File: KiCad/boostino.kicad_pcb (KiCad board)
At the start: 2 copper layers, 87.6 x 50.8 mm, 13 parts, among them J1 Conn_01x14_Female, J2 Conn_01x04_Male, Q1 2N3904, U1 Teensy3.6

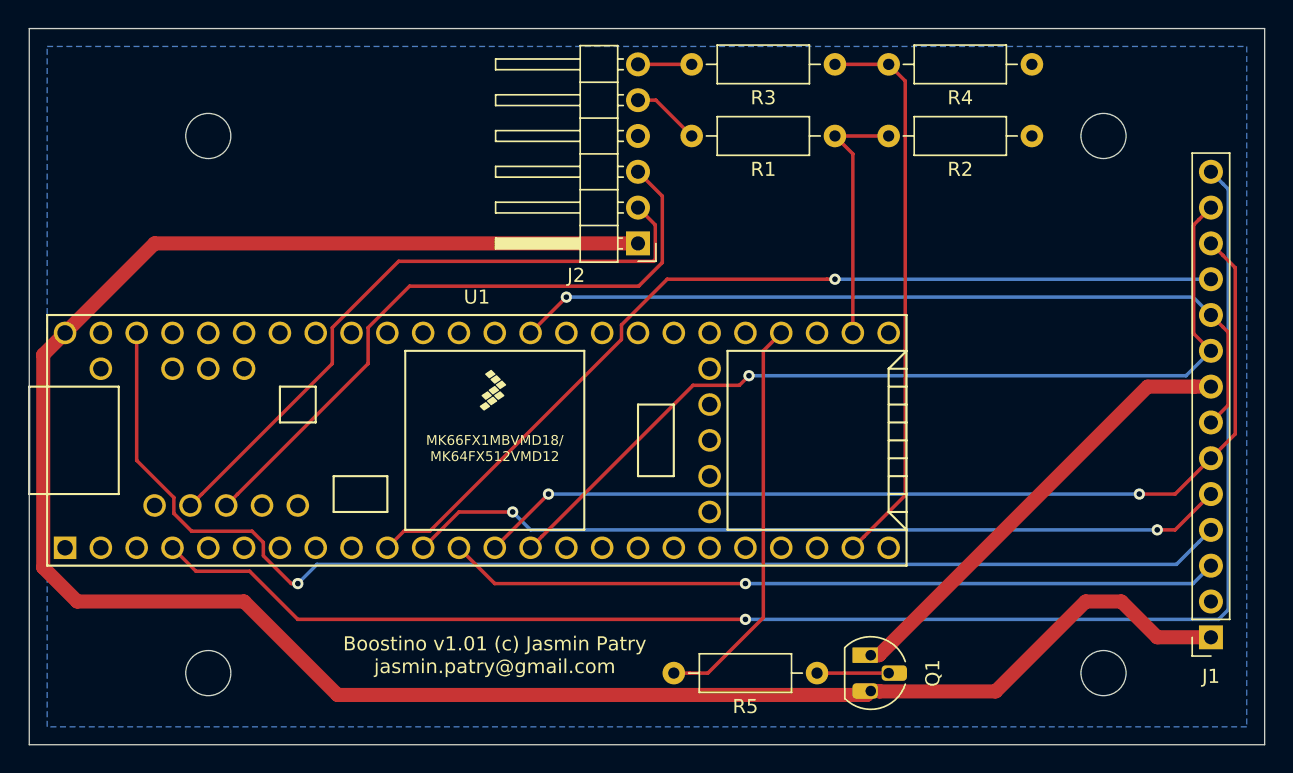
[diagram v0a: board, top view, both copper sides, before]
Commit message: Updated PCB for MC33660. Still need to regenerate Gerber files.
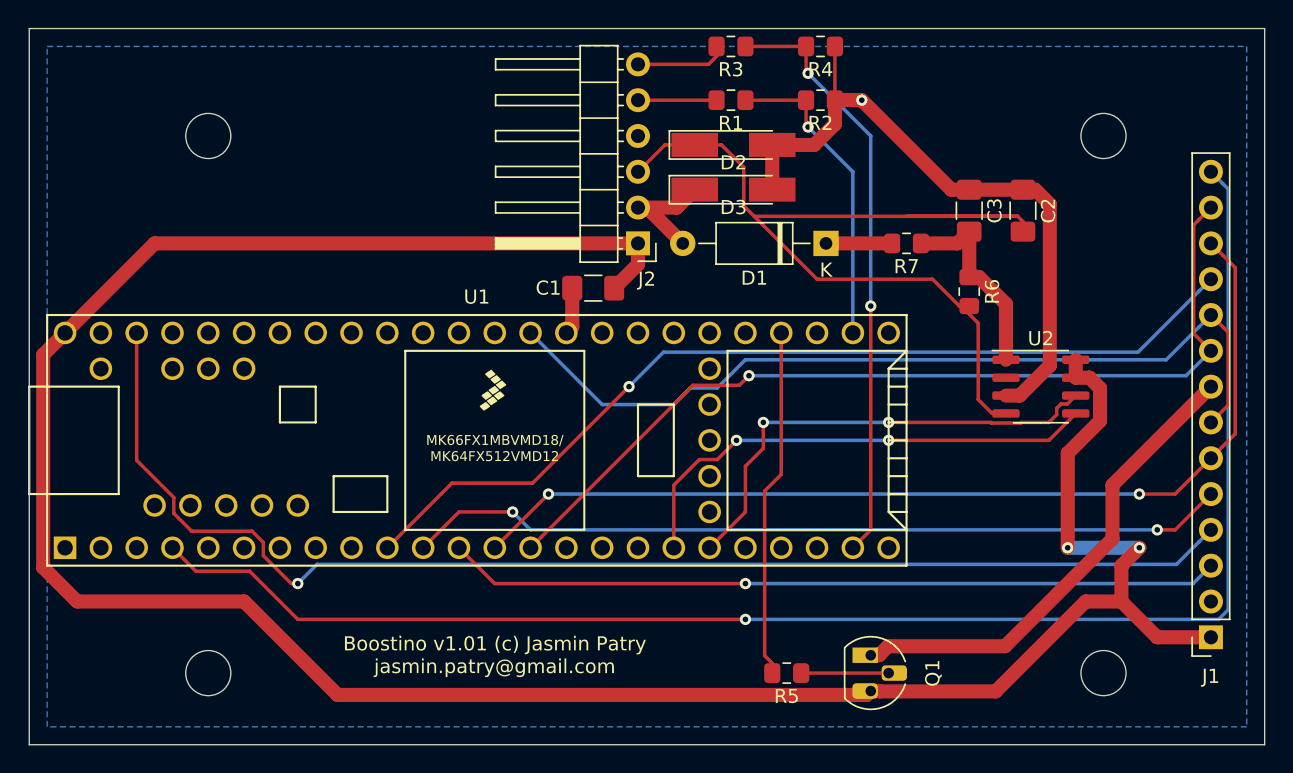
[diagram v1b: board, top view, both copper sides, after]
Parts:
- added C1: 1nF, Capacitor_SMD:C_1206_3216Metric_Pad1.42x1.75mm_HandSolder, F.Cu at (149.2, 101.0)
- added C2: 5nF, Capacitor_SMD:C_1206_3216Metric_Pad1.42x1.75mm_HandSolder, F.Cu at (179.7, 95.5)
- added C3: 10nF, Capacitor_SMD:C_1206_3216Metric_Pad1.42x1.75mm_HandSolder, F.Cu at (175.9, 95.5)
- added D1: D, Diode_THT:D_A-405_P10.16mm_Horizontal, F.Cu at (165.7, 97.8)
- added D2: D_Zener_27V, Diode_SMD:D_MiniMELF_Handsoldering, F.Cu at (159.2, 90.8)
- added D3: D_Zener_45V, Diode_SMD:D_MiniMELF_Handsoldering, F.Cu at (159.2, 94.0)
- added R6: 510, Resistor_SMD:R_0805_2012Metric_Pad1.15x1.40mm_HandSolder, F.Cu at (175.9, 101.2)
- added R7: 500, Resistor_SMD:R_0805_2012Metric_Pad1.15x1.40mm_HandSolder, F.Cu at (171.4, 97.8)
- added U2: MC33660, Package_SO:SOIC-8_3.9x4.9mm_P1.27mm, F.Cu at (181.0, 108.0)
- R1, R2, R3, R4, R5: footprint Resistor_THT:R_Axial_DIN0207_L6.3mm_D2.5mm_P10.16mm_Horizontal -> Resistor_SMD:R_0805_2012Metric_Pad1.15x1.40mm_HandSolder
- moved R2 15.2 mm to (165.3, 87.6)
- moved R4 15.0 mm to (165.3, 83.8)
- moved R1 7.80 mm to (159.0, 87.6)
- moved R3 7.48 mm to (159.0, 83.8)
- moved R5 2.15 mm to (162.9, 128.3)
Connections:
- J2 pad 2: /D- -> /VBAT
- J2 pad 3: /D+ -> /K_LINE
- U1 pad 18: Net-(U1-Pad18) -> /TX1
- U1 pad 19: Net-(U1-Pad19) -> /RX1
- U1 pad 59: /D- -> Net-(U1-Pad59)
- U1 pad 60: /D+ -> Net-(U1-Pad60)
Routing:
- net /K_LINE: track 0.00 -> 67.7 mm
- net /GND: track 0.00 -> 50.8 mm, vias 0 -> 1
- net /D+: track 46.7 -> 0.00 mm
- net /D-: track 45.9 -> 0.00 mm
- net /TX1: track 0.00 -> 35.1 mm, vias 0 -> 2
- net /RX1: track 0.00 -> 33.7 mm, vias 0 -> 2
- net /VCC: track 150.9 -> 179.8 mm, vias 0 -> 2
- net Net-(C3-Pad2): track 0.00 -> 14.3 mm
- net /VBAT: track 0.00 -> 8.78 mm
- net Net-(D1-Pad1): track 0.00 -> 4.69 mm
- net Net-(R1-Pad1): track 18.3 -> 22.2 mm, vias 0 -> 1
- net Net-(R5-Pad2): track 28.7 -> 24.8 mm
- net /SCK: track 58.5 -> 61.6 mm, vias 1 -> 0
- net Net-(J2-Pad6): track 3.81 -> 6.51 mm
- net /LED: track 32.0 -> 34.3 mm
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
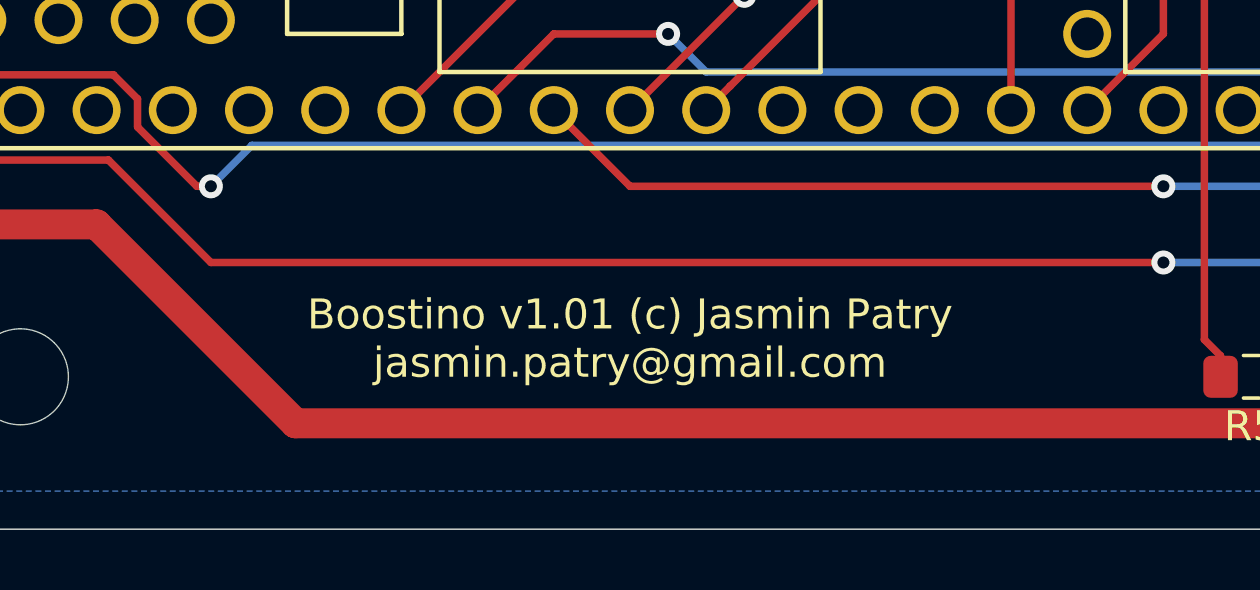
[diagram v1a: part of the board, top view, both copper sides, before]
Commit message: Generate Gerber files, bump PCB version to 2.0.
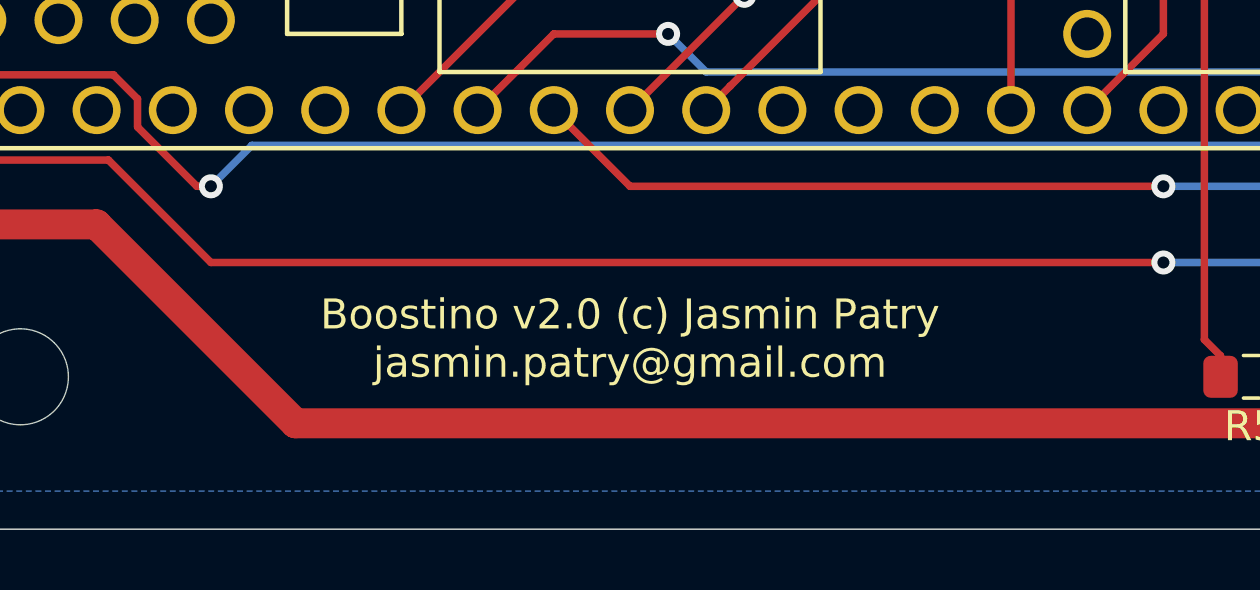
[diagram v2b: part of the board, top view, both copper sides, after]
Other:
- board text added: "Boostino v2.0 (c) Jasmin Patry jasmin.patry@gmail.com"
- board text removed: "Boostino v1.01 (c) Jasmin Patry jasmin.patry@gmail.com"
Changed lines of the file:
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@@
     )
   )
-  (gr_text "Boostino v1.01 (c) Jasmin Patry\njasmin.patry@gmail.com" (at 142.24 127) (layer F.SilkS)
+  (gr_text "Boostino v2.0 (c) Jasmin Patry\njasmin.patry@gmail.com" (at 142.24 127) (layer F.SilkS)
     (effects (font (size 1 1) (thickness 0.15)))
   )

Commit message: Update PCB to use Serial3 for K-Line
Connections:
- U1 pad 10: /T_CS -> /TX3
- U1 pad 18: /TX1 -> Net-(U1-Pad18)
- U1 pad 19: /RX1 -> Net-(U1-Pad19)
- U1 pad 6: Net-(U1-Pad6) -> /T_CS
- U1 pad 9: Net-(U1-Pad9) -> /RX3
- U2 pad 5: /TX1 -> /TX3
- U2 pad 6: /RX1 -> /RX3
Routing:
- net /RX3: track 0.00 -> 56.3 mm, vias 0 -> 1
- net /TX3: track 0.00 -> 52.8 mm, vias 0 -> 1
- net /TX1: track 35.1 -> 0.00 mm, vias 2 -> 0
- net /RX1: track 33.7 -> 0.00 mm, vias 2 -> 0
- net /T_CS: track 66.3 -> 79.6 mm, vias 1 -> 0
- net /RESET: track 91.6 -> 89.5 mm, vias 1 -> 0
- net /SCK: track 61.6 -> 60.6 mm
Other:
- board text added: "Boostino v2.01 (c) Jasmin Patry jasmin.patry@gmail.com"
- board text removed: "Boostino v2.0 (c) Jasmin Patry jasmin.patry@gmail.com"
